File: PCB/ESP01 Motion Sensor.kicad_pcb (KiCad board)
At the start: 2 copper layers, 48.9 x 31.8 mm, 10 parts, among them J1 USB POWER, J2 Conn_01x03_Female, SW1 SW_Push, U1 NCP1117-3.3, U2 ESP-01

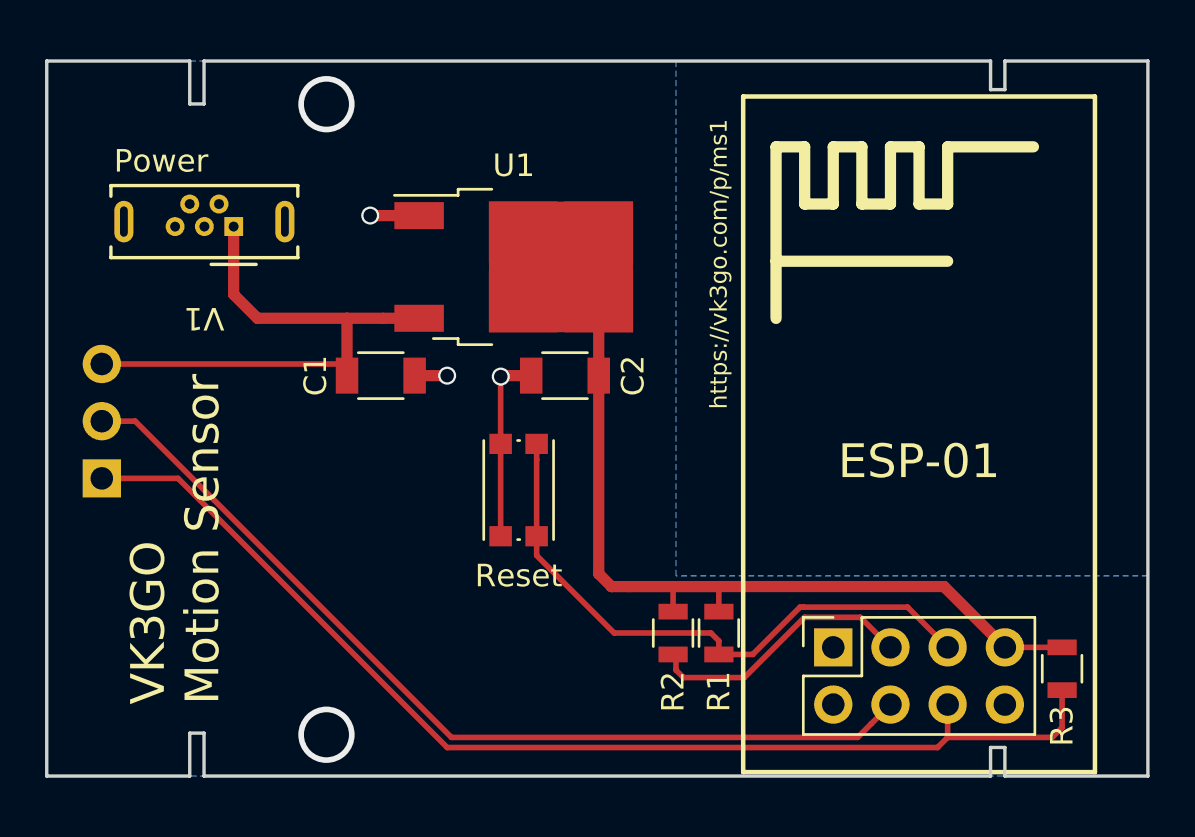
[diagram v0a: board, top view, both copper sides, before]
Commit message: Fix ESP-01 pinout, rotate motion sensor module, make board 33x49mm, make mounting cutouts larger
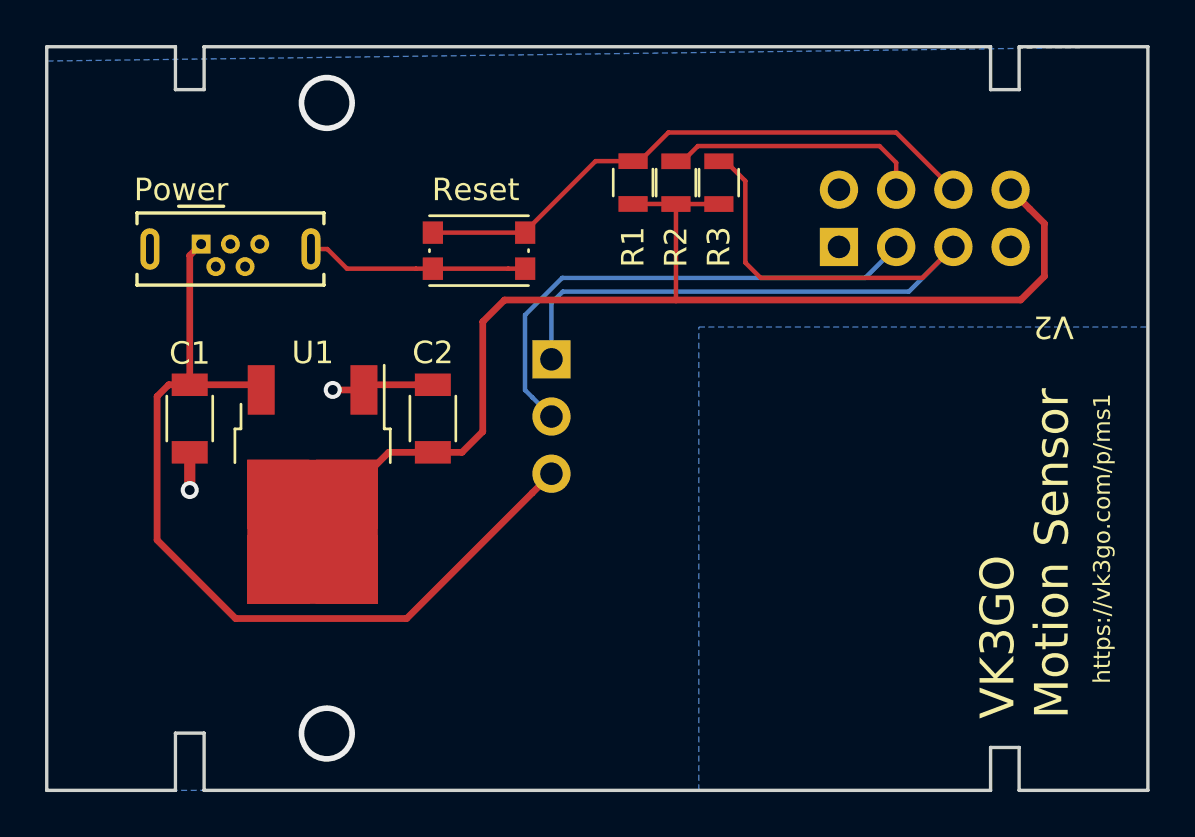
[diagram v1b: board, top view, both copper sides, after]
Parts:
- U2: moved to B.Cu
- moved R3 26.4 mm to (142.2, 88.0), turned to 270 degrees
- moved J2 20.7 mm to (134.8, 95.8), turned to 180 degrees
- moved R1 20.4 mm to (138.4, 87.9), turned to 270 degrees
- moved R2 20.0 mm to (140.3, 88.0), turned to 270 degrees
- moved U2 17.8 mm to (147.6, 90.8), turned to 270 degrees
- moved U1 13.2 mm to (124.2, 101.4), turned to 270 degrees
- moved SW1 10.8 mm to (131.6, 91.0), turned to 0 degrees
- moved C1 8.70 mm to (118.7, 98.4), turned to 270 degrees
- moved C2 6.17 mm to (129.5, 98.4), turned to 90 degrees
- moved J1 1.64 mm to (119.3, 90.7), turned to 0 degrees
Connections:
- U2 pad 1: Net-(U2-Pad1) -> GND
- U2 pad 2: GND -> Net-(U2-Pad2)
- U2 pad 3: /CH_PD -> /GPIO2
- U2 pad 4: /GPIO2 -> /CH_PD
- U2 pad 5: /RST -> /GPIO0
- U2 pad 6: /GPIO0 -> /RST
- U2 pad 7: +3V3 -> Net-(U2-Pad7)
- U2 pad 8: Net-(U2-Pad8) -> +3V3
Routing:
- net /GPIO2: track 41.4 -> 22.7 mm
- net /GPIO0: track 51.1 -> 36.6 mm
- net +3V3: track 36.4 -> 50.4 mm
- net +5V: track 25.5 -> 39.1 mm
- net GND: track 12.1 -> 15.8 mm, vias 3 -> 2
- net /RST: track 27.0 -> 25.7 mm
- net /CH_PD: track 12.0 -> 11.3 mm
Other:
- board size 48.9 x 31.8 mm -> 48.9 x 33 mm
- net class Default: trace_width 0.25 -> 0.2
- net class Power: trace_width 0.5 -> 0.3
- board text added: "V2"
- board text removed: "V1"
